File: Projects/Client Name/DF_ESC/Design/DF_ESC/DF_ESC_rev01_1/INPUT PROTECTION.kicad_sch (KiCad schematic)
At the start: 13 parts, among them J7 XT60PW-M

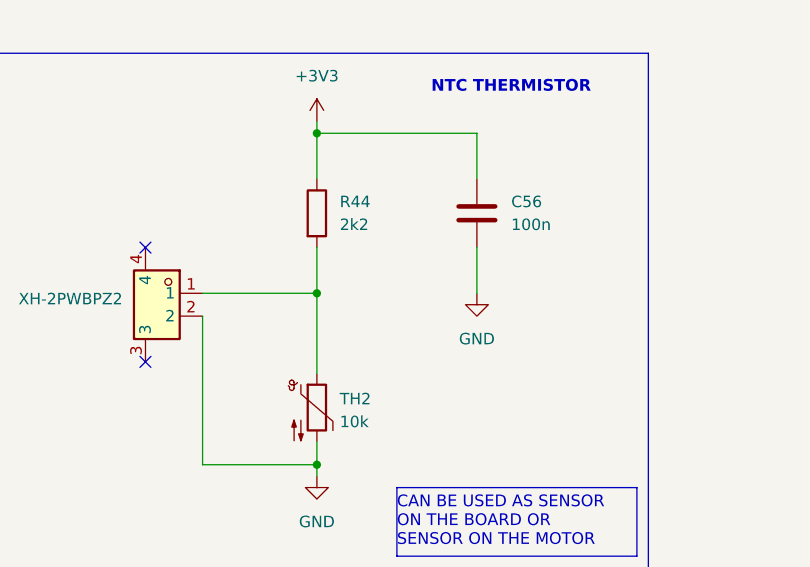
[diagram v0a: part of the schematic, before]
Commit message: updated footprints
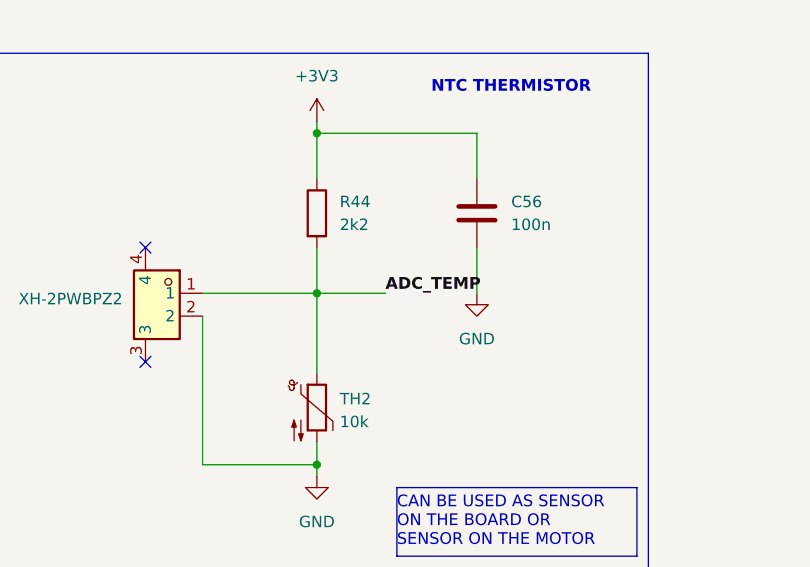
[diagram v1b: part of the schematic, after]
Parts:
- C55, C57: footprint (none) -> Capacitor_SMD:CP_Elec_6.3x5.4_Nichicon
- C56: footprint (none) -> Capacitor_SMD:C_0201_0603Metric
- C58: footprint (none) -> Capacitor_SMD:C_0603_1608Metric
- D12: footprint (none) -> LED_SMD:LED_1W_3W_R8
- R44, R45, R46, R47: footprint (none) -> Resistor_SMD:R_0201_0603Metric
- TH2: footprint (none) -> Resistor_SMD:R_0805_2012Metric
- XH-2PWBPZ2: footprint (none) -> XT60PW-M:AMASS_XT60PW-M
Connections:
- net ADC_TEMP: now also R44.2, TH2.1, XH-2PWBPZ2.1
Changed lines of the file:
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@@
+	(wire
+		(pts
+			(xy 101.6 135.89) (xy 109.22 135.89)
+		)
+		(stroke
+			(width 0)
+			(type default)
+		)
+	)
 	(wire
 		(pts
@@
 			(font
 				(size 1.27 1.27)
+			)
+			(justify left bottom)
+		)
+	)
+	(label "ADC_TEMP"
+		(at 109.22 135.89 0)
+		(effects
+			(font
+				(size 1.3 1.3)
+				(thickness 0.26)
+				(bold yes)
+				(color 0 0 0 1)
 			)
 			(justify left bottom)
@@
 			)
 		)
-		(property "Footprint" ""
+		(property "Footprint" "Capacitor_SMD:C_0603_1608Metric"
 			(at 182.5752 90.17 0)
 			(effects
@@
 			)
 		)
-		(property "Footprint" ""
+		(property "Footprint" "Capacitor_SMD:CP_Elec_6.3x5.4_Nichicon"
 			(at 133.35 80.01 0)
 			(effects
@@
 			)
 		)
-		(property "Footprint" ""
+		(property "Footprint" "Resistor_SMD:R_0201_0603Metric"
 			(at 99.822 127 90)
 			(effects
@@
 			)
 		)
-		(property "Footprint" ""
+		(property "Footprint" "Capacitor_SMD:C_0201_0603Metric"
 			(at 120.3452 130.81 0)
 			(effects
@@
 			)
 		)
-		(property "Footprint" ""
+		(property "Footprint" "XT60PW-M:AMASS_XT60PW-M"
 			(at 87.63 130.81 0)
 			(effects
@@
 			)
 		)
-		(property "Footprint" ""
+		(property "Footprint" "Resistor_SMD:R_0201_0603Metric"
 			(at 169.672 86.36 90)
 			(effects
@@
 			)
 		)
-		(property "Footprint" ""
+		(property "Footprint" "LED_SMD:LED_1W_3W_R8"
 			(at 222.25 83.82 0)
 			(effects
@@
 			)
 		)
-		(property "Footprint" ""
+		(property "Footprint" "Resistor_SMD:R_0201_0603Metric"
 			(at 169.672 73.66 90)
 			(effects
@@
 			)
 		)
-		(property "Footprint" ""
+		(property "Footprint" "Capacitor_SMD:CP_Elec_6.3x5.4_Nichicon"
 			(at 144.78 80.01 0)
 			(effects
@@
 			)
 		)
-		(property "Footprint" ""
+		(property "Footprint" "Resistor_SMD:R_0805_2012Metric"
 			(at 101.6 147.32 0)
 			(effects
@@
 			)
 		)
-		(property "Footprint" ""
+		(property "Footprint" "Resistor_SMD:R_0201_0603Metric"
 			(at 220.472 71.12 90)
 			(effects
